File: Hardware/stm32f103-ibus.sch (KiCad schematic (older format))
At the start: 14 parts

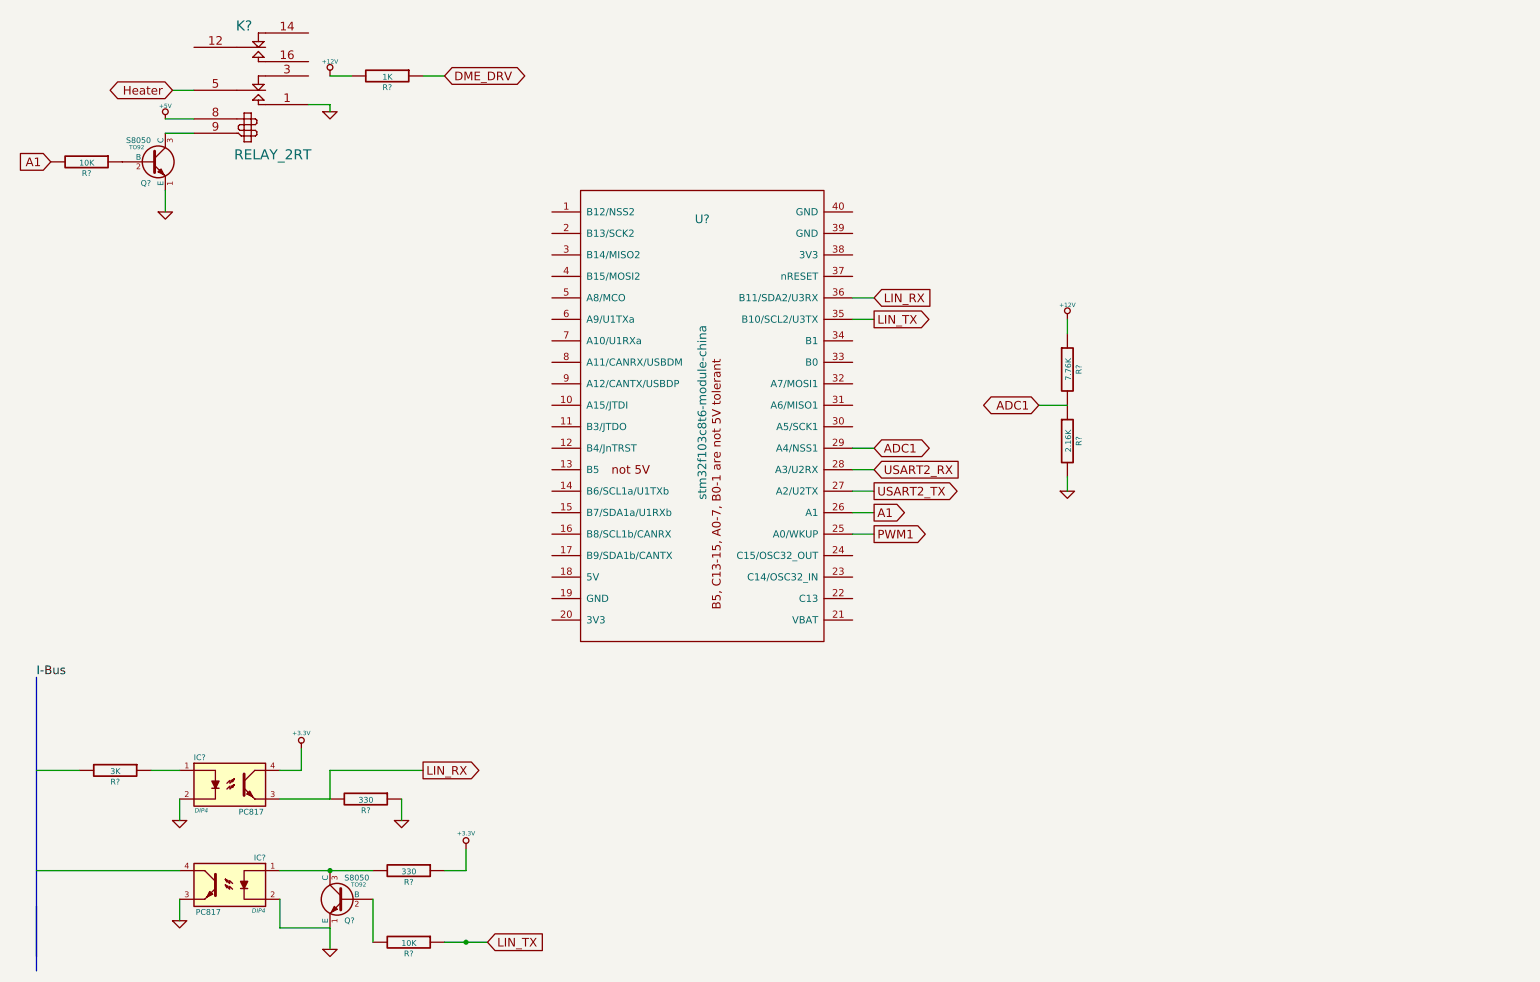
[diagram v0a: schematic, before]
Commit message: 1.PWM1 signal level shift to 12V 2.Supports PWM reverse
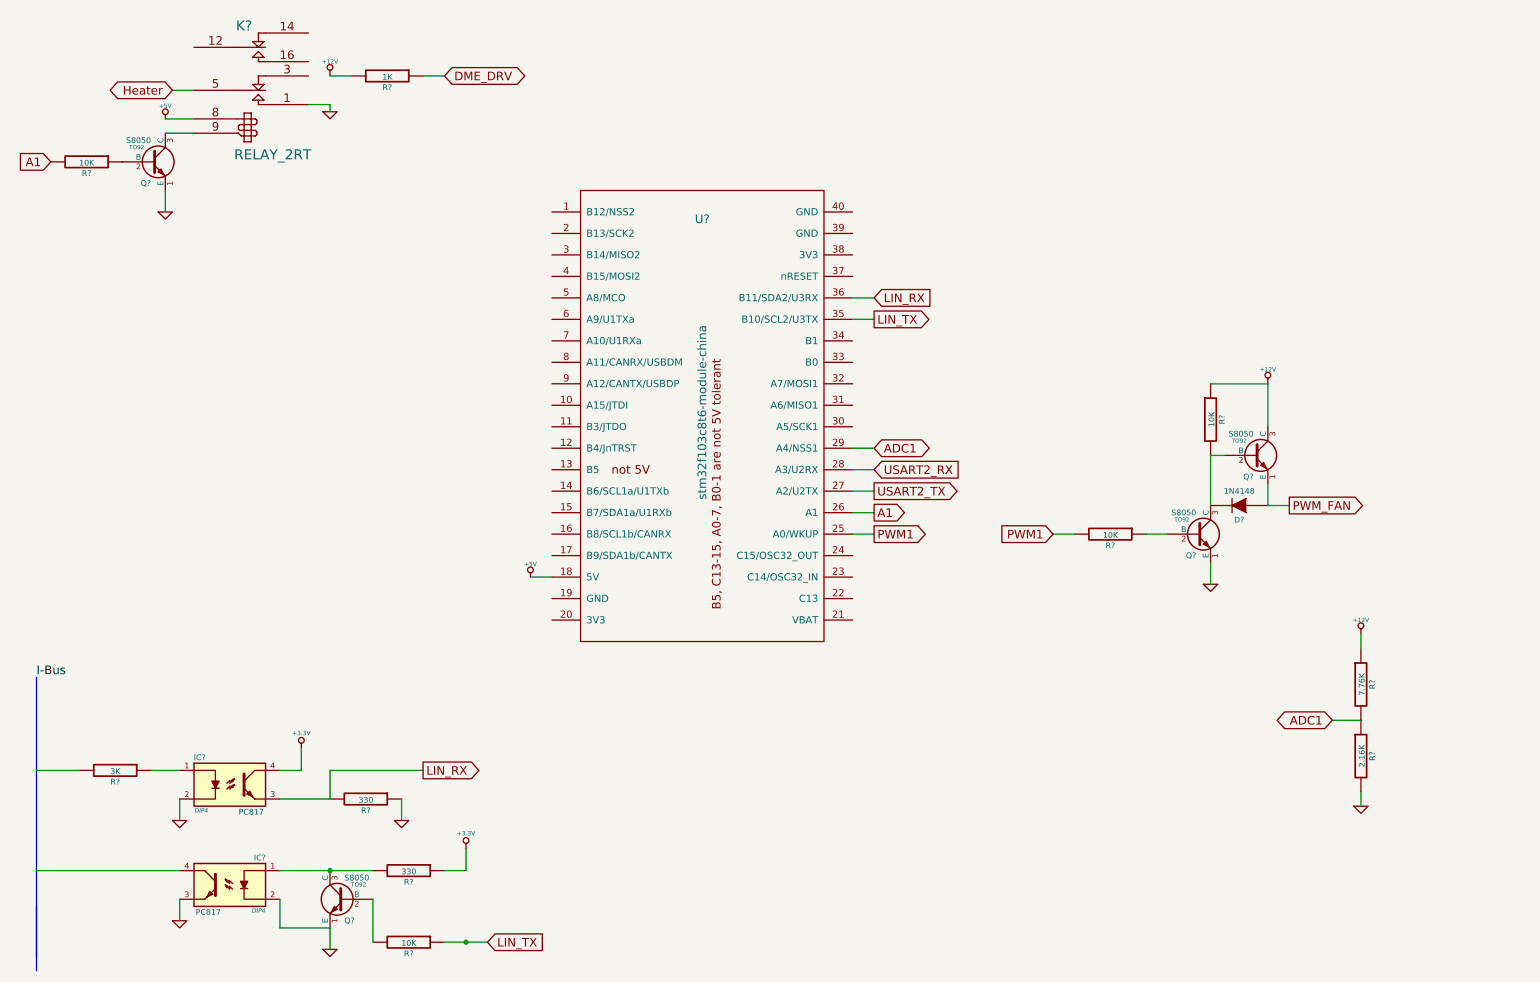
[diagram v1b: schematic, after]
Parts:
- added D?: 1N4148, symbol DIODE
- added Q? (x2): S8050, TO92, symbol S8050
- added R? (x2): 10K, symbol R
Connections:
- net labels added: PWM_FAN
- wire segments 37 -> 47
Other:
- moved on the sheet: R?
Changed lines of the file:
@@
 L R R?
 U 1 1 5964BF5E
-P 8000 3150
-F 0 "R?" V 8080 3150 40  0000 C CNN
-F 1 "7.76K" V 8007 3151 40  0000 C CNN
-F 2 "" V 7930 3150 30  0000 C CNN
-F 3 "" H 8000 3150 30  0000 C CNN
-	1    8000 3150
+P 10050 5350
+F 0 "R?" V 10130 5350 40  0000 C CNN
+F 1 "7.76K" V 10057 5351 40  0000 C CNN
+F 2 "" V 9980 5350 30  0000 C CNN
+F 3 "" H 10050 5350 30  0000 C CNN
+	1    10050 5350
 	1    0    0    -1
 $EndComp
@@
 L R R?
 U 1 1 5964BF77
-P 8000 3650
-F 0 "R?" V 8080 3650 40  0000 C CNN
-F 1 "2.16K" V 8007 3651 40  0000 C CNN
-F 2 "" V 7930 3650 30  0000 C CNN
-F 3 "" H 8000 3650 30  0000 C CNN
-	1    8000 3650
+P 10050 5850
+F 0 "R?" V 10130 5850 40  0000 C CNN
+F 1 "2.16K" V 10057 5851 40  0000 C CNN
+F 2 "" V 9980 5850 30  0000 C CNN
+F 3 "" H 10050 5850 30  0000 C CNN
+	1    10050 5850
 	1    0    0    -1
 $EndComp
@@
 L +12V #PWR?
 U 1 1 5964C013
-P 8000 2800
-F 0 "#PWR?" H 8000 2750 20  0001 C CNN
-F 1 "+12V" H 8000 2900 30  0000 C CNN
-F 2 "" H 8000 2800 60  0000 C CNN
-F 3 "" H 8000 2800 60  0000 C CNN
-	1    8000 2800
+P 10050 5000
+F 0 "#PWR?" H 10050 4950 20  0001 C CNN
+F 1 "+12V" H 10050 5100 30  0000 C CNN
+F 2 "" H 10050 5000 60  0000 C CNN
+F 3 "" H 10050 5000 60  0000 C CNN
+	1    10050 5000
 	1    0    0    -1
 $EndComp
@@
 L GND #PWR?
 U 1 1 5964C07B
-P 8000 4000
-F 0 "#PWR?" H 8000 4000 30  0001 C CNN
-F 1 "GND" H 8000 3930 30  0001 C CNN
-F 2 "" H 8000 4000 60  0000 C CNN
-F 3 "" H 8000 4000 60  0000 C CNN
-	1    8000 4000
-	1    0    0    -1
-$EndComp
-Text GLabel 7800 3400 0    60   BiDi ~ 0
+P 10050 6200
+F 0 "#PWR?" H 10050 6200 30  0001 C CNN
+F 1 "GND" H 10050 6130 30  0001 C CNN
+F 2 "" H 10050 6200 60  0000 C CNN
+F 3 "" H 10050 6200 60  0000 C CNN
+	1    10050 6200
+	1    0    0    -1
+$EndComp
+Text GLabel 9850 5600 0    60   BiDi ~ 0
 ADC1
 Text GLabel 1750 1200 0    60   BiDi ~ 0
@@
 	6500 3700 6650 3700
 Wire Wire Line
-	8000 2800 8000 2900
-Wire Wire Line
-	8000 3900 8000 4000
-Wire Wire Line
-	7800 3400 8000 3400
+	10050 5000 10050 5100
+Wire Wire Line
+	10050 6100 10050 6200
+Wire Wire Line
+	9850 5600 10050 5600
 Wire Wire Line
 	1700 1900 1700 2050
@@
 Wire Wire Line
 	2700 1300 2850 1300
+$Comp
+L +5V #PWR?
+U 1 1 598D88F3
+P 4250 4600
+F 0 "#PWR?" H 4250 4690 20  0001 C CNN
+F 1 "+5V" H 4250 4690 30  0000 C CNN
+F 2 "" H 4250 4600 60  0000 C CNN
+F 3 "" H 4250 4600 60  0000 C CNN
+	1    4250 4600
+	1    0    0    -1
+$EndComp
+Wire Wire Line
+	4400 4600 4250 4600
+Text GLabel 7900 4300 0    60   Input ~ 0
+PWM1
+$Comp
+L R R?
+U 1 1 598D90CA
+P 8300 4300
+F 0 "R?" V 8380 4300 40  0000 C CNN
+F 1 "10K" V 8307 4301 40  0000 C CNN
+F 2 "" V 8230 4300 30  0000 C CNN
+F 3 "" H 8300 4300 30  0000 C CNN
+	1    8300 4300
+	0    1    1    0
+$EndComp
+$Comp
+L S8050 Q?
+U 1 1 598D916B
+P 8900 4300
+F 0 "Q?" H 8900 4151 40  0000 R CNN
+F 1 "S8050" H 8900 4450 40  0000 R CNN
+F 2 "TO92" H 8800 4402 29  0000 C CNN
+F 3 "" H 8900 4300 60  0000 C CNN
+	1    8900 4300
+	1    0    0    -1
+$EndComp
+$Comp
+L S8050 Q?
+U 1 1 598D918C
+P 9300 3750
+F 0 "Q?" H 9300 3601 40  0000 R CNN
+F 1 "S8050" H 9300 3900 40  0000 R CNN
+F 2 "TO92" H 9200 3852 29  0000 C CNN
+F 3 "" H 9300 3750 60  0000 C CNN
+	1    9300 3750
+	1    0    0    -1
+$EndComp
+$Comp
+L DIODE D?
+U 1 1 598D91BF
+P 9200 4100
+F 0 "D?" H 9200 4200 40  0000 C CNN
+F 1 "1N4148" H 9200 4000 40  0000 C CNN
+F 2 "" H 9200 4100 60  0000 C CNN
+F 3 "" H 9200 4100 60  0000 C CNN
+	1    9200 4100
+	-1   0    0    1
+$EndComp
+$Comp
+L R R?
+U 1 1 598D93C9
+P 9000 3500
+F 0 "R?" V 9080 3500 40  0000 C CNN
+F 1 "10K" V 9007 3501 40  0000 C CNN
+F 2 "" V 8930 3500 30  0000 C CNN
+F 3 "" H 9000 3500 30  0000 C CNN
+	1    9000 3500
+	1    0    0    -1
+$EndComp
+$Comp
+L +12V #PWR?
+U 1 1 598D9443
+P 9400 3250
+F 0 "#PWR?" H 9400 3200 20  0001 C CNN
+F 1 "+12V" H 9400 3350 30  0000 C CNN
+F 2 "" H 9400 3250 60  0000 C CNN
+F 3 "" H 9400 3250 60  0000 C CNN
+	1    9400 3250
+	1    0    0    -1
+$EndComp
+Wire Wire Line
+	9400 3250 9000 3250
+Wire Wire Line
+	9000 3750 9100 3750
+Wire Wire Line
+	9400 3250 9400 3550
+Wire Wire Line
+	9000 3750 9000 4100
+Wire Wire Line
+	9400 3950 9400 4100
+Wire Wire Line
+	7900 4300 8050 4300
+Wire Wire Line
+	8550 4300 8700 4300
+$Comp
+L GND #PWR?
+U 1 1 598D9625
+P 9000 4650
+F 0 "#PWR?" H 9000 4650 30  0001 C CNN
+F 1 "GND" H 9000 4580 30  0001 C CNN
+F 2 "" H 9000 4650 60  0000 C CNN
+F 3 "" H 9000 4650 60  0000 C CNN
+	1    9000 4650
+	1    0    0    -1
+$EndComp
+Wire Wire Line
+	9000 4500 9000 4650
+Text GLabel 9550 4100 2    60   Output ~ 0
+PWM_FAN
+Wire Wire Line
+	9400 4100 9550 4100
 $EndSCHEMATC

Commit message: 1.Modify H/W circuit to make more detail 2.Add README.ADC 3.Support ADC1 channel5 on PA5 4.Minor fix of logic of target thermostat temperature
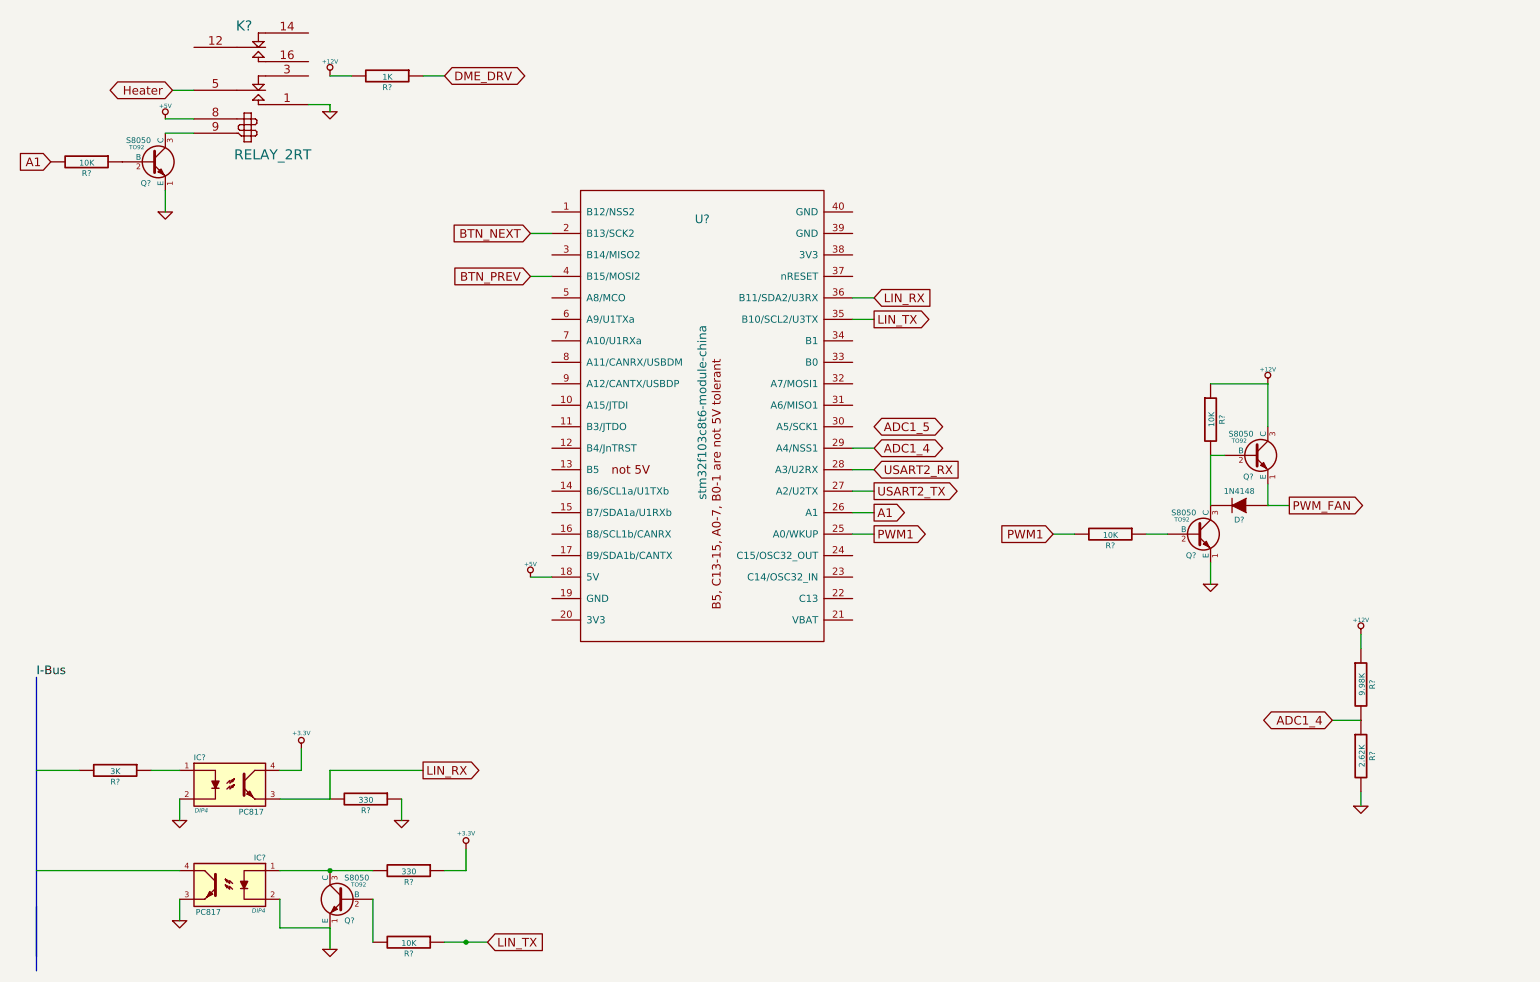
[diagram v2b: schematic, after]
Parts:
- R?: value 7.76K -> 9.98K
- R?: value 2.16K -> 2.62K
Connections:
- net labels added: ADC1_4, ADC1_5, BTN_NEXT, BTN_PREV
- net labels removed: ADC1
- wire segments 47 -> 49
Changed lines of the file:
@@
 $EndComp
 Text GLabel 6650 3700 2    60   BiDi ~ 0
-ADC1
+ADC1_4
 $Comp
 L R R?
@@
 P 10050 5350
 F 0 "R?" V 10130 5350 40  0000 C CNN
-F 1 "7.76K" V 10057 5351 40  0000 C CNN
+F 1 "9.98K" V 10057 5351 40  0000 C CNN
 F 2 "" V 9980 5350 30  0000 C CNN
 F 3 "" H 10050 5350 30  0000 C CNN
@@
 P 10050 5850
 F 0 "R?" V 10130 5850 40  0000 C CNN
-F 1 "2.16K" V 10057 5851 40  0000 C CNN
+F 1 "2.62K" V 10057 5851 40  0000 C CNN
 F 2 "" V 9980 5850 30  0000 C CNN
 F 3 "" H 10050 5850 30  0000 C CNN
@@
 $EndComp
 Text GLabel 9850 5600 0    60   BiDi ~ 0
-ADC1
+ADC1_4
 Text GLabel 1750 1200 0    60   BiDi ~ 0
 Heater
@@
 Wire Wire Line
 	9400 4100 9550 4100
+Text GLabel 6650 3550 2    60   BiDi ~ 0
+ADC1_5
+Text GLabel 4250 2200 0    60   Input ~ 0
+BTN_NEXT
+Text GLabel 4250 2500 0    60   Input ~ 0
+BTN_PREV
+Wire Wire Line
+	4250 2200 4400 2200
+Wire Wire Line
+	4250 2500 4400 2500
 $EndSCHEMATC

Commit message: 1.Add documents for low side current sense 2.Add datasheet of LM358 3.Supports ADC1 channel 5 to detect thermostat heater current 4.Display thermostat heater current 5.Various update
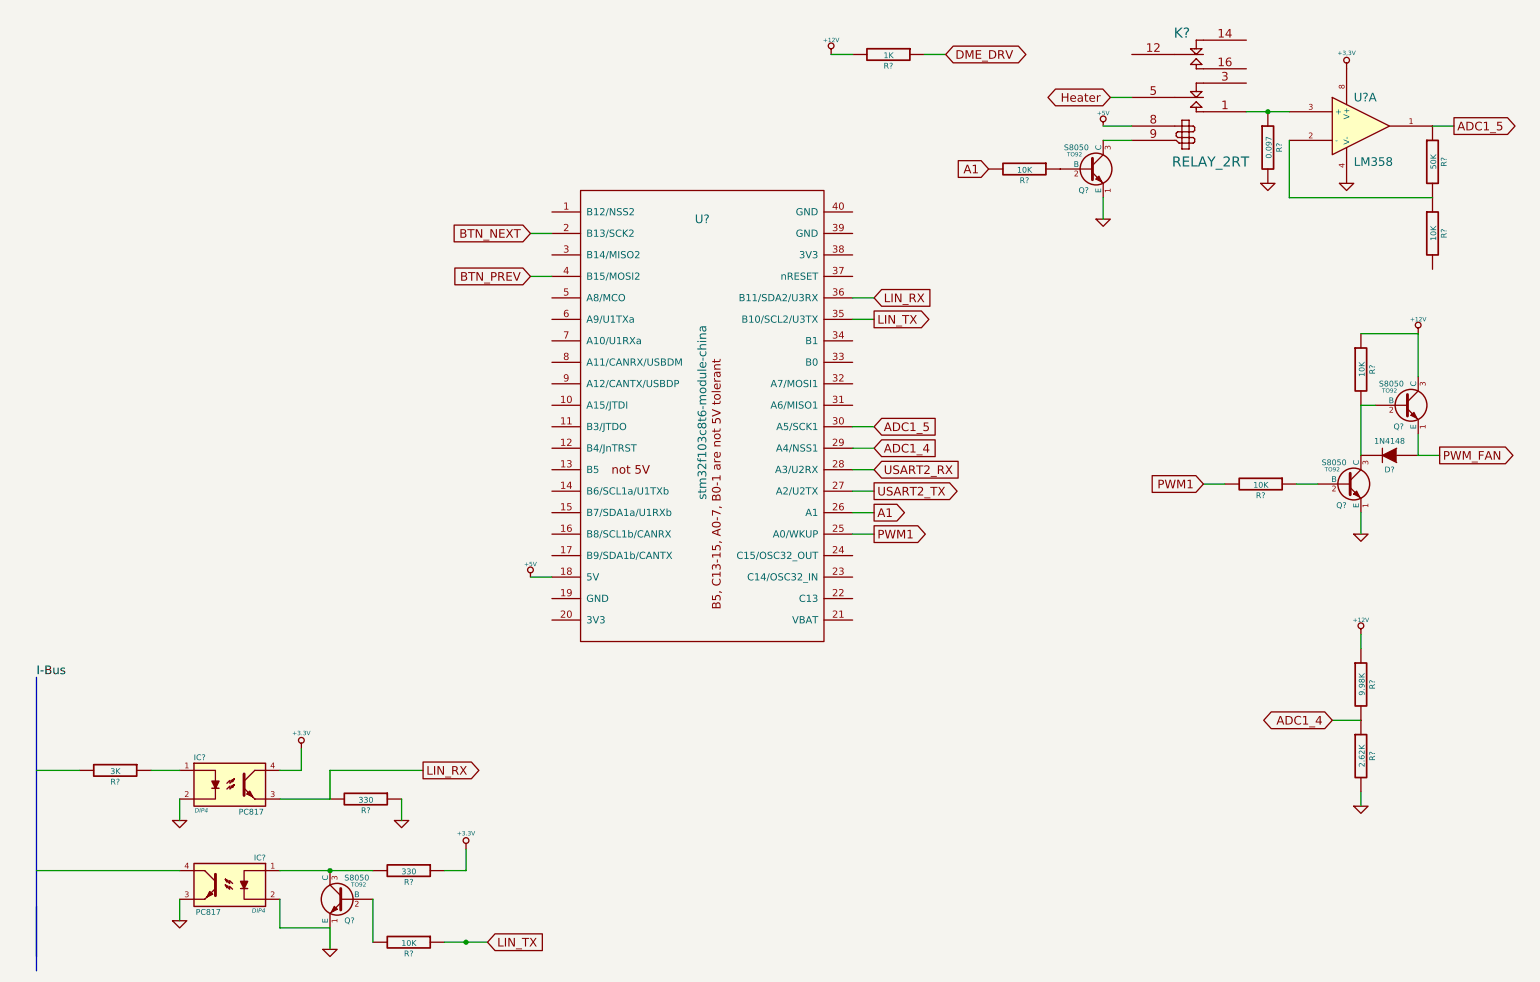
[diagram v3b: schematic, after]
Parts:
- added R?: 50K, symbol R
- added R?: 10K, symbol R
- added R?: 0.097, symbol R
- added U?: LM358, symbol LM358
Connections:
- net labels added: +3,3V
- wire segments 49 -> 52
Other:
- moved on the sheet: D?, K?, Q?, R?
